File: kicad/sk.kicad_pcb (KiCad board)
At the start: 2 copper layers, 233 x 130 mm, 95 parts, among them J1 AC, J2 Barrel_Jack, J3 Barrel_Jack, J4 Barrel_Jack, J5 Barrel_Jack, J6 Barrel_Jack, J7 Barrel_Jack, SW1 SW_DIP_x01, SW2 SW_DIP_x01, SW3 SW_DIP_x01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

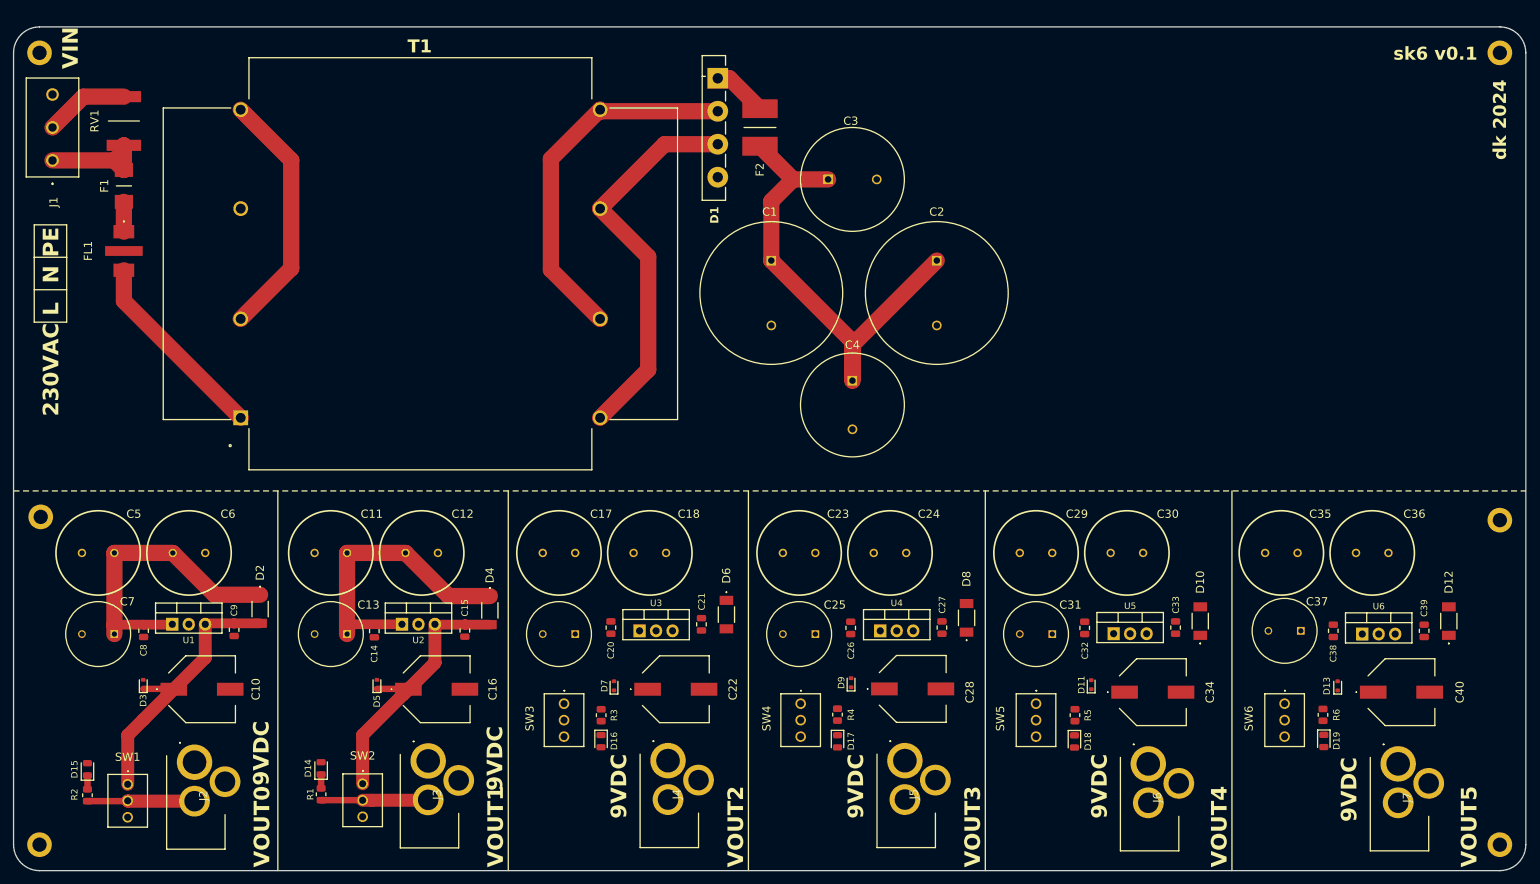
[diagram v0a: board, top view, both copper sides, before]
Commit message: Add more PCB routings
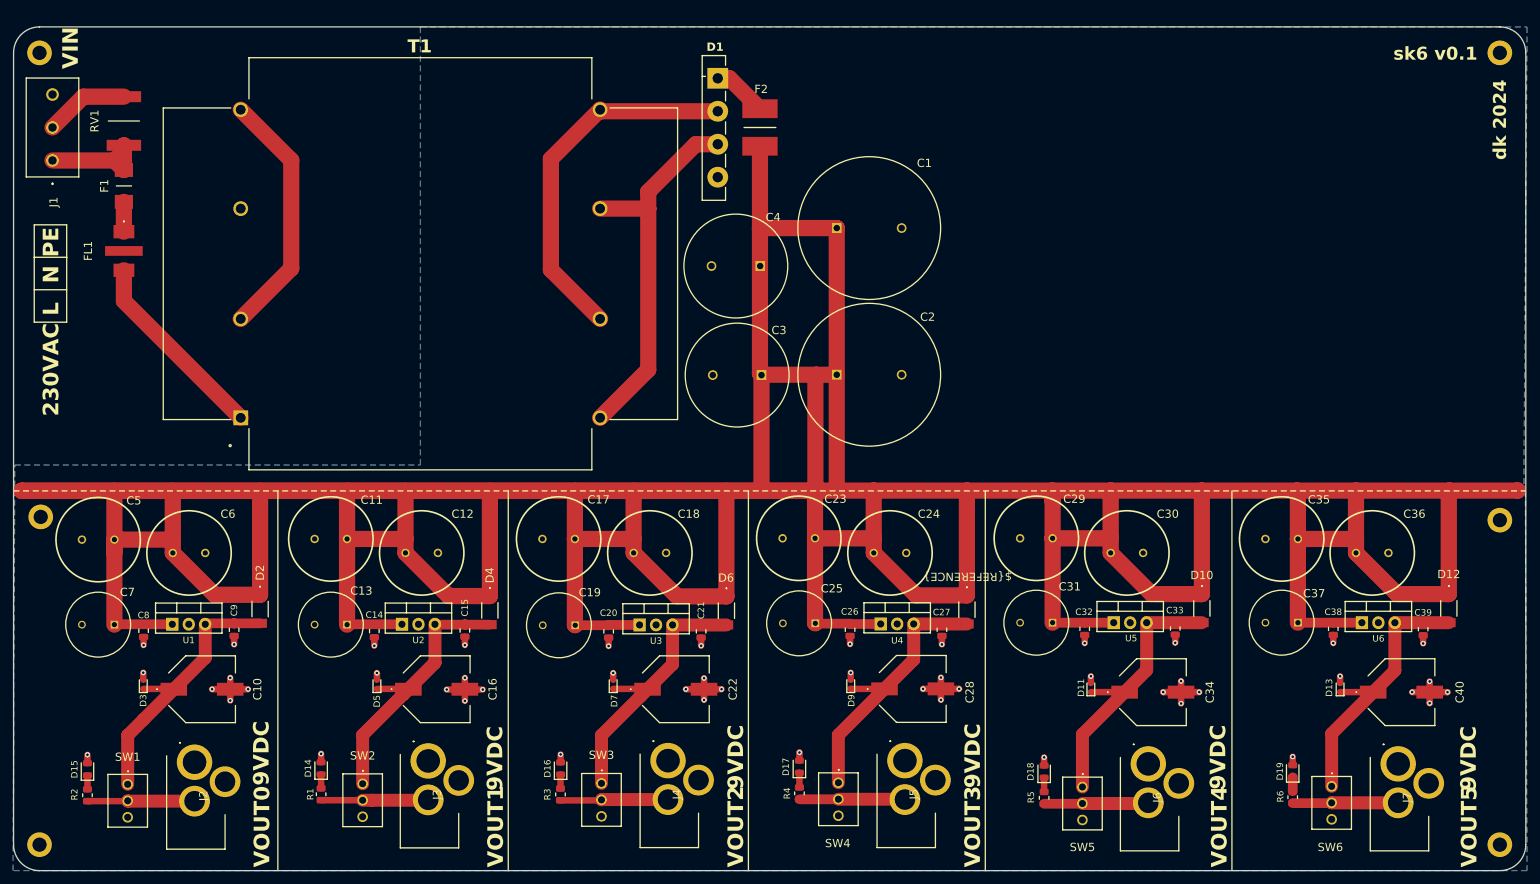
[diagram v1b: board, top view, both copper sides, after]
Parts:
- moved C3 31.8 mm to (135.1, 76.2), turned to 180 degrees
- moved C2 23.4 mm to (146.7, 76.1), turned to 0 degrees
- moved C4 22.7 mm to (134.8, 59.4), turned to 180 degrees
- moved SW5 14.7 mm to (184.5, 139.6)
- moved SW6 14.7 mm to (222.9, 139.5)
- moved R3 13.7 mm to (104.1, 140.8), turned to 90 degrees
- moved R5 13.6 mm to (178.6, 141.3)
- moved SW3 13.6 mm to (110.4, 139.1)
- moved R6 13.5 mm to (216.9, 141.2)
- moved SW4 13.5 mm to (146.9, 139.0)
- moved R4 13.5 mm to (140.9, 140.6)
- moved C1 11.3 mm to (146.7, 53.5), turned to 0 degrees
- moved D16 7.52 mm to (104.1, 136.8), turned to 90 degrees
- moved D17 7.06 mm to (140.9, 136.5), turned to 90 degrees
- moved D19 6.69 mm to (216.9, 137.2), turned to 90 degrees
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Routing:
- net /230VAC/+12VDC: track 166.4 -> 977.9 mm
- net GND: track 0.00 -> 83.1 mm, vias 0 -> 48
- net /9VDC5/+9VDC: track 0.00 -> 43.1 mm
- net /9VDC6/+9VDC: track 0.00 -> 42.7 mm
- net /9VDC4/+9VDC: track 0.00 -> 42.7 mm
- net /9VDC3/+9VDC: track 0.00 -> 42.6 mm
- net /IND3/VOUT: track 0.00 -> 16.6 mm
- net /IND4/VOUT: track 0.00 -> 16.3 mm
- net /IND6/VOUT: track 0.00 -> 16.3 mm
- net /IND5/VOUT: track 0.00 -> 16.1 mm
- net Net-(D17-K): track 0.00 -> 2.26 mm
- net Net-(D18-K): track 0.00 -> 2.19 mm
- net Net-(D16-K): track 0.00 -> 2.16 mm
- net Net-(D19-K): track 0.00 -> 2.15 mm
- net /230VAC/TOUT+: track 60.6 -> 59.1 mm
- added copper zone on B.Cu, net GND
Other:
- board text added: "${REFERENCE}"

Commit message: Make PCB rework
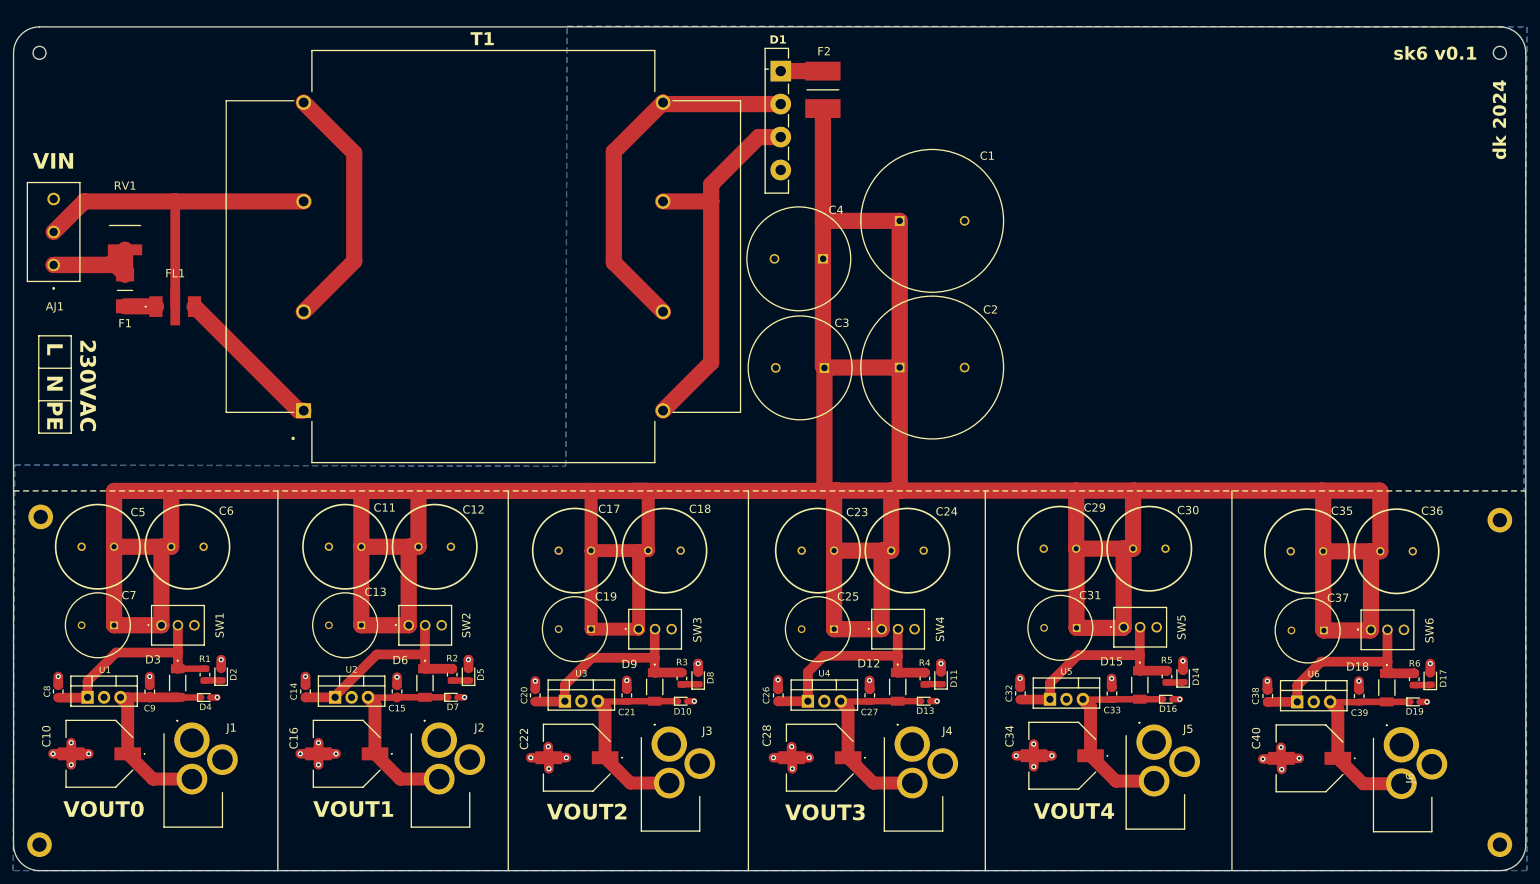
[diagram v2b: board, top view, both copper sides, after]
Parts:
- removed J7: Barrel_Jack, barrel-jack:PJ002A
- added J1: Barrel_Jack, barrel-jack:PJ002A, F.Cu at (47.3, 132.4)
- D10, D4: value D -> D_TVS; footprint diode:SE8D20DHM3H -> Diode_SMD:D_SOD-523
- D11, D5: value D_TVS -> LED; footprint Diode_SMD:D_SOD-523 -> Diode_SMD:D_0805_2012Metric
- D15, D18: value LED -> D; footprint Diode_SMD:D_0805_2012Metric -> diode:SE8D20DHM3H
- D16, D19: value LED -> D_TVS; footprint Diode_SMD:D_0805_2012Metric -> Diode_SMD:D_SOD-523
- D2, D8: value D -> LED; footprint diode:SE8D20DHM3H -> Diode_SMD:D_0805_2012Metric
- D3, D9: value D_TVS -> D; footprint Diode_SMD:D_SOD-523 -> diode:SE8D20DHM3H
- H3, H6: value MountingHole_Pad -> MountingHole; footprint MountingHole:MountingHole_2.2mm_M2_ISO14580_Pad -> MountingHole:MountingHole_2mm
- moved D15 162.7 mm to (193.3, 123.9), turned to -90 degrees
- moved D14 133.6 mm to (200.0, 122.5)
- moved D17 98.1 mm to (238.1, 122.9)
- moved D16 94.1 mm to (197.6, 126.1), turned to 0 degrees
- moved D12 85.8 mm to (156.0, 124.2)
- moved D10 81.3 mm to (122.9, 126.4), turned to 0 degrees
- moved D13 63.9 mm to (160.3, 126.4), turned to 0 degrees
- moved R2 59.2 mm to (87.4, 122.3), turned to -90 degrees
- moved D18 54.4 mm to (231.4, 124.3), turned to -90 degrees
- moved D6 47.8 mm to (83.2, 123.6)
- moved D4 45.8 mm to (49.4, 125.8), turned to 0 degrees
- moved D8 42.7 mm to (125.3, 122.9), turned to 90 degrees
- moved J6 39.1 mm to (233.6, 133.1)
- moved J5 38.5 mm to (195.5, 132.7)
- moved J2 37.9 mm to (85.4, 132.4)
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- renumbered J1 to AJ1
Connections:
- C14 pad 1: /230VAC/+12VDC -> Net-(D6-K)
- C20 pad 1: /230VAC/+12VDC -> Net-(D9-K)
- C26 pad 1: /230VAC/+12VDC -> Net-(D12-K)
- C32 pad 1: /230VAC/+12VDC -> Net-(D15-K)
- C38 pad 1: /230VAC/+12VDC -> Net-(D18-K)
- C8 pad 1: /230VAC/+12VDC -> Net-(D3-K)
- D10 pad 1: /230VAC/+12VDC -> /9VDC3/+9VDC
- D10 pad 2: /9VDC5/+9VDC -> GND
- D11 pad 1: /9VDC5/+9VDC -> Net-(D11-K)
- D12 pad 1: /230VAC/+12VDC -> Net-(D12-K)
- D12 pad 2: /9VDC6/+9VDC -> /9VDC4/+9VDC
- D13 pad 1: /9VDC6/+9VDC -> /9VDC4/+9VDC
- D15 pad 2: GND -> /9VDC5/+9VDC
- D16 pad 1: Net-(D16-K) -> /9VDC5/+9VDC
- D18 pad 2: GND -> /9VDC6/+9VDC
- D19 pad 1: Net-(D19-K) -> /9VDC6/+9VDC
- D2 pad 1: /230VAC/+12VDC -> Net-(D2-K)
- D2 pad 2: /9VDC1/+9VDC -> GND
- D3 pad 1: /9VDC1/+9VDC -> Net-(D3-K)
- D3 pad 2: GND -> /9VDC1/+9VDC
- D4 pad 1: /230VAC/+12VDC -> /9VDC1/+9VDC
- D4 pad 2: /9VDC2/+9VDC -> GND
- D5 pad 1: /9VDC2/+9VDC -> Net-(D5-K)
- D6 pad 1: /230VAC/+12VDC -> Net-(D6-K)
- D6 pad 2: /9VDC3/+9VDC -> /9VDC2/+9VDC
- D7 pad 1: /9VDC3/+9VDC -> /9VDC2/+9VDC
- D8 pad 1: /230VAC/+12VDC -> Net-(D8-K)
- D8 pad 2: /9VDC4/+9VDC -> GND
- D9 pad 1: /9VDC4/+9VDC -> Net-(D9-K)
- D9 pad 2: GND -> /9VDC3/+9VDC
- J2 pad 2: /IND1/VOUT -> /9VDC2/+9VDC
- J3 pad 2: /IND2/VOUT -> /9VDC3/+9VDC
- J4 pad 2: /IND3/VOUT -> /9VDC4/+9VDC
- J5 pad 2: /IND4/VOUT -> /9VDC5/+9VDC
- J6 pad 2: /IND5/VOUT -> /9VDC6/+9VDC
- R1 pad 1: /IND2/VOUT -> Net-(D3-K)
- R1 pad 2: Net-(D14-K) -> Net-(D2-K)
- R2 pad 1: /IND1/VOUT -> Net-(D6-K)
- R2 pad 2: Net-(D15-K) -> Net-(D5-K)
- R3 pad 1: /IND3/VOUT -> Net-(D9-K)
- R3 pad 2: Net-(D16-K) -> Net-(D8-K)
- R4 pad 1: /IND4/VOUT -> Net-(D12-K)
- R4 pad 2: Net-(D17-K) -> Net-(D11-K)
- R5 pad 1: /IND5/VOUT -> Net-(D15-K)
- R5 pad 2: Net-(D18-K) -> Net-(D14-K)
- R6 pad 1: /IND6/VOUT -> Net-(D18-K)
- R6 pad 2: Net-(D19-K) -> Net-(D17-K)
- SW1 pad 1: /9VDC1/+9VDC -> /230VAC/+12VDC
- SW1 pad 2: /IND1/VOUT -> Net-(D3-K)
- SW2 pad 1: /9VDC2/+9VDC -> /230VAC/+12VDC
- SW2 pad 2: /IND2/VOUT -> Net-(D6-K)
- SW3 pad 1: /9VDC3/+9VDC -> /230VAC/+12VDC
- SW3 pad 2: /IND3/VOUT -> Net-(D9-K)
- SW4 pad 1: /9VDC4/+9VDC -> /230VAC/+12VDC
- SW4 pad 2: /IND4/VOUT -> Net-(D12-K)
- SW5 pad 1: /9VDC5/+9VDC -> /230VAC/+12VDC
- SW5 pad 2: /IND5/VOUT -> Net-(D15-K)
- SW6 pad 1: /9VDC6/+9VDC -> /230VAC/+12VDC
- SW6 pad 2: /IND6/VOUT -> Net-(D18-K)
- U1 pad 1: /230VAC/+12VDC -> Net-(D3-K)
- U2 pad 1: /230VAC/+12VDC -> Net-(D6-K)
- U3 pad 1: /230VAC/+12VDC -> Net-(D9-K)
- U4 pad 1: /230VAC/+12VDC -> Net-(D12-K)
- U5 pad 1: /230VAC/+12VDC -> Net-(D15-K)
- U6 pad 1: /230VAC/+12VDC -> Net-(D18-K)
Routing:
- net /230VAC/+12VDC: track 977.9 -> 671.7 mm
- net /230VAC/NEUTRAL: track 13.0 -> 56.7 mm
- net Net-(D12-K): track 0.00 -> 34.9 mm
- net Net-(D3-K): track 0.00 -> 33.7 mm
- net Net-(D9-K): track 0.00 -> 33.6 mm
- net Net-(D6-K): track 0.00 -> 32.2 mm
- net Net-(D15-K): track 2.15 -> 33.6 mm
- net Net-(D18-K): track 2.19 -> 33.5 mm
- net /IND2/VOUT: track 17.9 -> 0.00 mm
- net /IND3/VOUT: track 16.6 -> 0.00 mm
- net /IND1/VOUT: track 16.5 -> 0.00 mm
- net /9VDC2/+9VDC: track 49.6 -> 33.1 mm
- net /IND4/VOUT: track 16.3 -> 0.00 mm
- net /IND6/VOUT: track 16.3 -> 0.00 mm
- net /IND5/VOUT: track 16.1 -> 0.00 mm
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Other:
- board text removed: "${REFERENCE}"
- board text removed: "9VDC"
- board text removed: "SW1"
- board text removed: "VOUT5"

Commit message: Enhance PCB
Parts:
- moved F1 14.6 mm to (49.3, 71.0)
- moved C22 14.6 mm to (118.9, 142.9)
- moved C26 14.6 mm to (149.9, 133.3)
- moved C28 14.6 mm to (156.3, 142.9)
- moved C31 14.6 mm to (195.9, 122.9)
- moved C40 14.6 mm to (231.8, 143.0)
- moved D16 14.6 mm to (209.9, 133.9)
- moved J4 14.6 mm to (170.6, 140.8)
- moved R6 14.6 mm to (247.9, 130.8)
- moved U5 14.6 mm to (191.8, 133.9)
- moved U6 14.6 mm to (229.9, 134.3)
- moved C1 14.6 mm to (168.7, 60.2)
- moved C10 14.6 mm to (45.4, 142.3)
- moved C5 14.6 mm to (45.1, 110.4)
- moved C18 14.6 mm to (132.4, 111.0)
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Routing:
- net /230VAC/+12VDC: track 671.7 -> 0.00 mm
- net GND: track 84.8 -> 16.5 mm, vias 48 -> 81
- net /230VAC/TOUT+: track 59.1 -> 0.00 mm
- net /230VAC/NEUTRAL: track 56.7 -> 0.00 mm
- net /230VAC/TOUT-: track 56.7 -> 0.34 mm
- net Net-(T1-Pad2): track 38.7 -> 0.00 mm
- net /9VDC1/+9VDC: track 33.2 -> 0.03 mm
- net /9VDC3/+9VDC: track 33.1 -> 0.07 mm
- net /9VDC4/+9VDC: track 33.1 -> 0.07 mm
- net /9VDC2/+9VDC: track 33.1 -> 0.12 mm
- net /9VDC5/+9VDC: track 33.0 -> 0.07 mm
- net /9VDC6/+9VDC: track 33.0 -> 0.14 mm
- net /230VAC/+230VAC: track 27.4 -> 0.00 mm
- net Net-(FL1-Pad2): track 23.5 -> 0.00 mm
- net /230VAC/DOUT+: track 6.50 -> 0.00 mm
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- added copper zone on F.Cu, net /230VAC/+12VDC
- added copper zone on F.Cu, net /230VAC/+230VAC
- added copper zone on F.Cu, net /230VAC/DOUT+
- added copper zone on F.Cu, net /230VAC/NEUTRAL
- added copper zone on F.Cu, net /230VAC/TOUT+
- added copper zone on F.Cu, net /230VAC/TOUT-
- added copper zone on F.Cu, net /9VDC1/+9VDC
- added copper zone on F.Cu, net /9VDC2/+9VDC
- added copper zone on F.Cu, net /9VDC3/+9VDC
- added copper zone on F.Cu, net /9VDC4/+9VDC
- added copper zone on F.Cu, net /9VDC5/+9VDC
- added copper zone on F.Cu, net /9VDC6/+9VDC
- added copper zone on F.Cu, net GND
- added copper zone on F.Cu, net Net-(F1-Pad2)
- added copper zone on F.Cu, net Net-(FL1-Pad2)
- added copper zone on F.Cu, net Net-(T1-Pad2)
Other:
- board size 233 x 130 mm -> 226.5 x 121.5 mm
- board text added: "VOUT5"

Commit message: Enhance PCB
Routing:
- net /230VAC/NEUTRAL: track 0.00 -> 54.7 mm
- net Net-(T1-Pad2): track 0.00 -> 38.8 mm
- net Net-(FL1-Pad2): track 0.00 -> 23.5 mm
- net Net-(F1-Pad2): track 0.00 -> 4.76 mm
- net GND: vias 81 -> 145
- removed copper zone on F.Cu, net /230VAC/NEUTRAL
- removed copper zone on F.Cu, net Net-(F1-Pad2)
- removed copper zone on F.Cu, net Net-(FL1-Pad2)
- removed copper zone on F.Cu, net Net-(T1-Pad2)
